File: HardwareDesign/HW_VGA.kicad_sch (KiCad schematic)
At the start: 6 parts, among them J1 Conn_02x40_Odd_Even, J401 Conn_01x06, U1 25.175 MHz, U301 GAL22V10

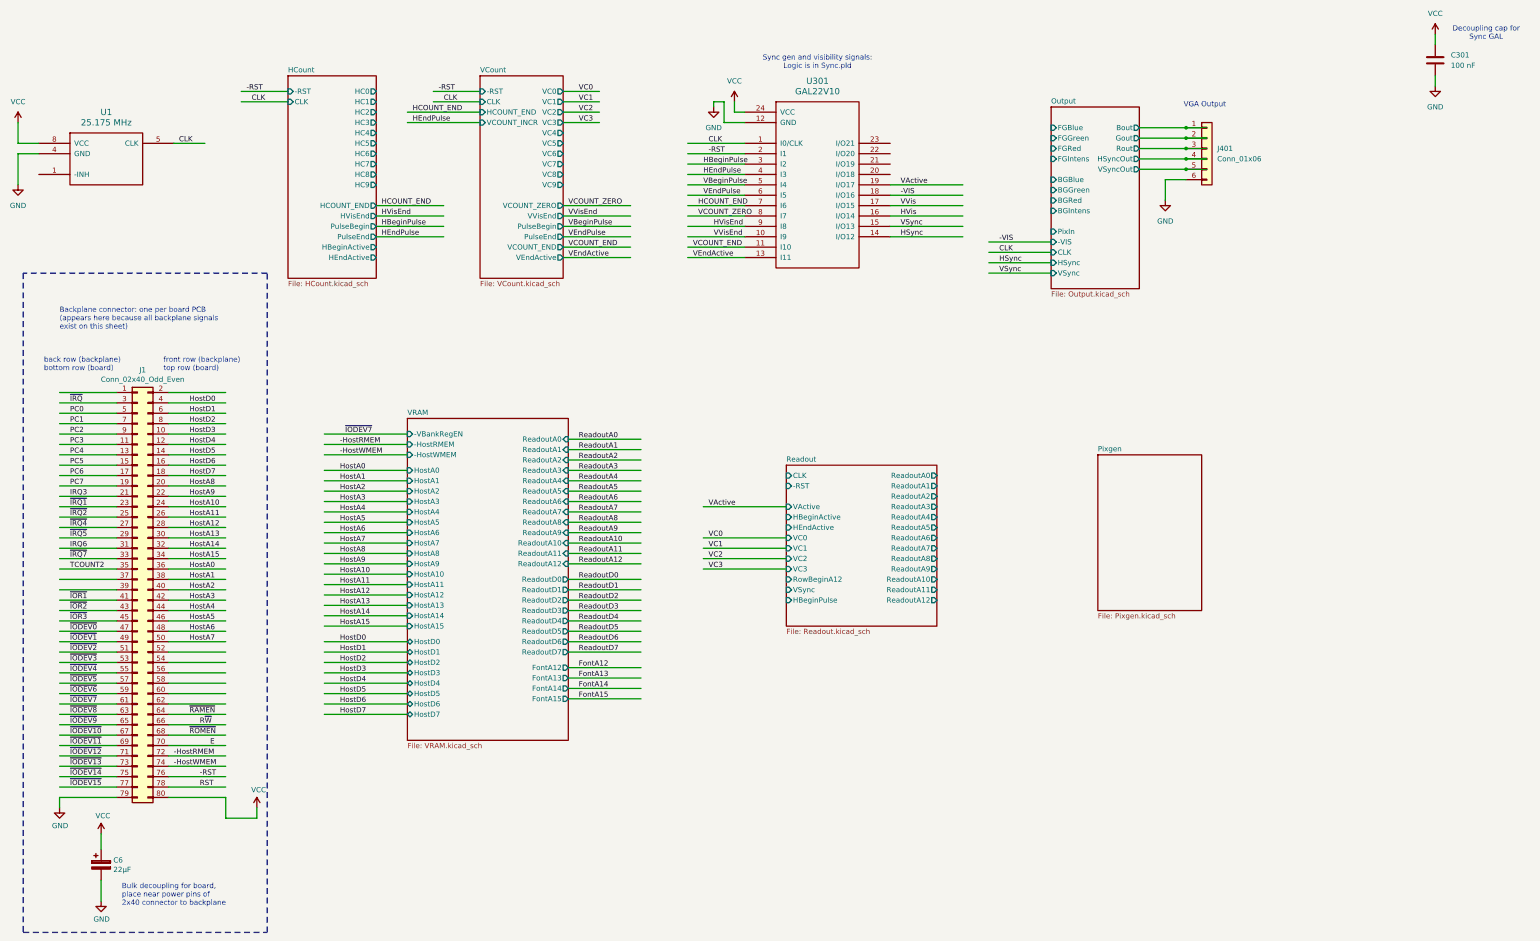
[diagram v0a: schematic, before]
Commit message: more main sheet cleanups
Also removed one unneeded pin (ReadoutA12) for the
Readout module: it's a purely internal signal.
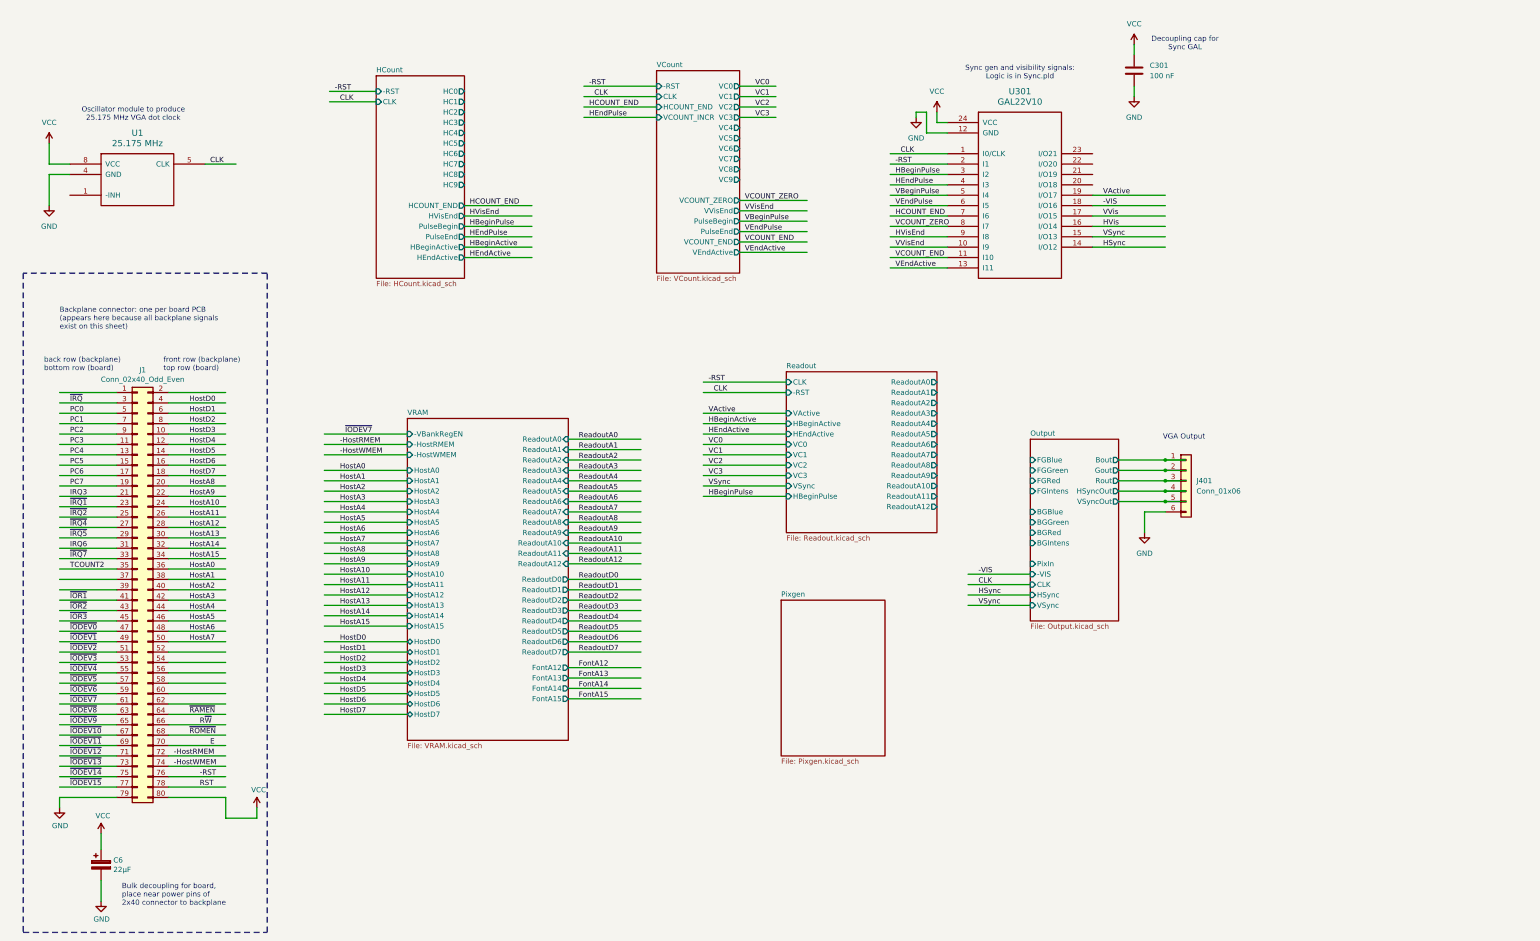
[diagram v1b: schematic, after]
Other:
- sheet Readout ports: added none; removed RowBeginA12
- note added: "Oscillator module to produce 25.175 MHz VGA dot clock"
- moved on the sheet: C301, J401, U1, U301

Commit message: a few more main sheet cleanups
At this point I think most/all of the changes to
the simulation are reflected in the schematic. Need
to go over everything carefully to make sure.
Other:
- note added: "Horizontal count"
- note added: "Readout module (generate addresses for reading character and attribute data from VRAM)"
- note added: "VRAM (video memory for character and attribute data)"
- note added: "Vertical count"
- moved on the sheet: J401, U1

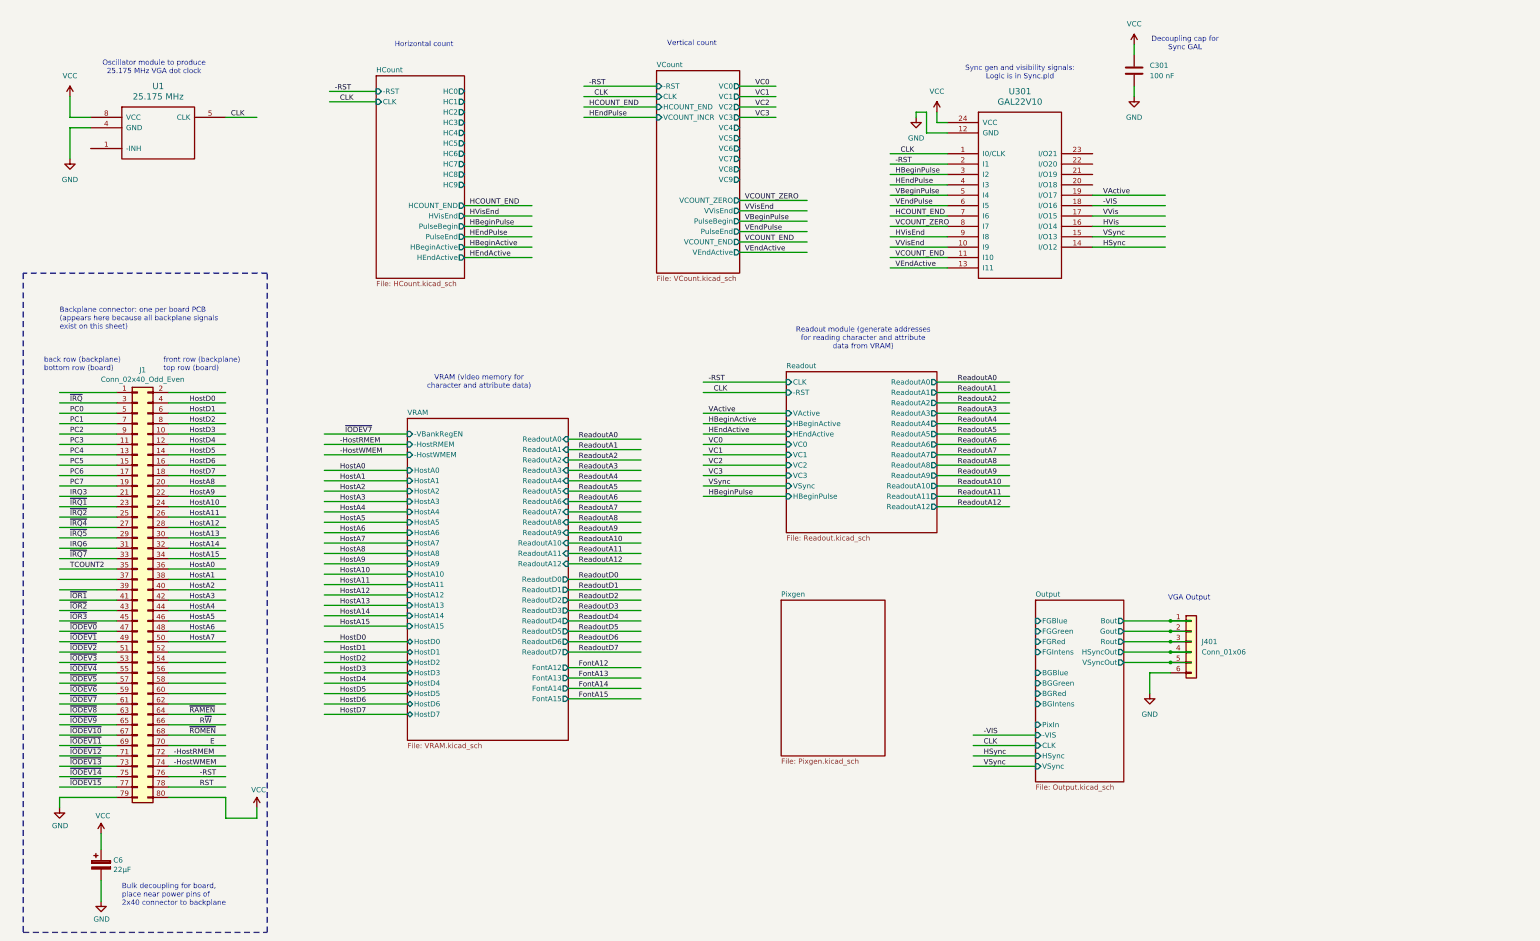
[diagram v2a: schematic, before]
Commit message: much work on pixel generation schematic, logic
In theory, this is potentially a complete hardware design,
but need to simulate it to make sure it will actually work.
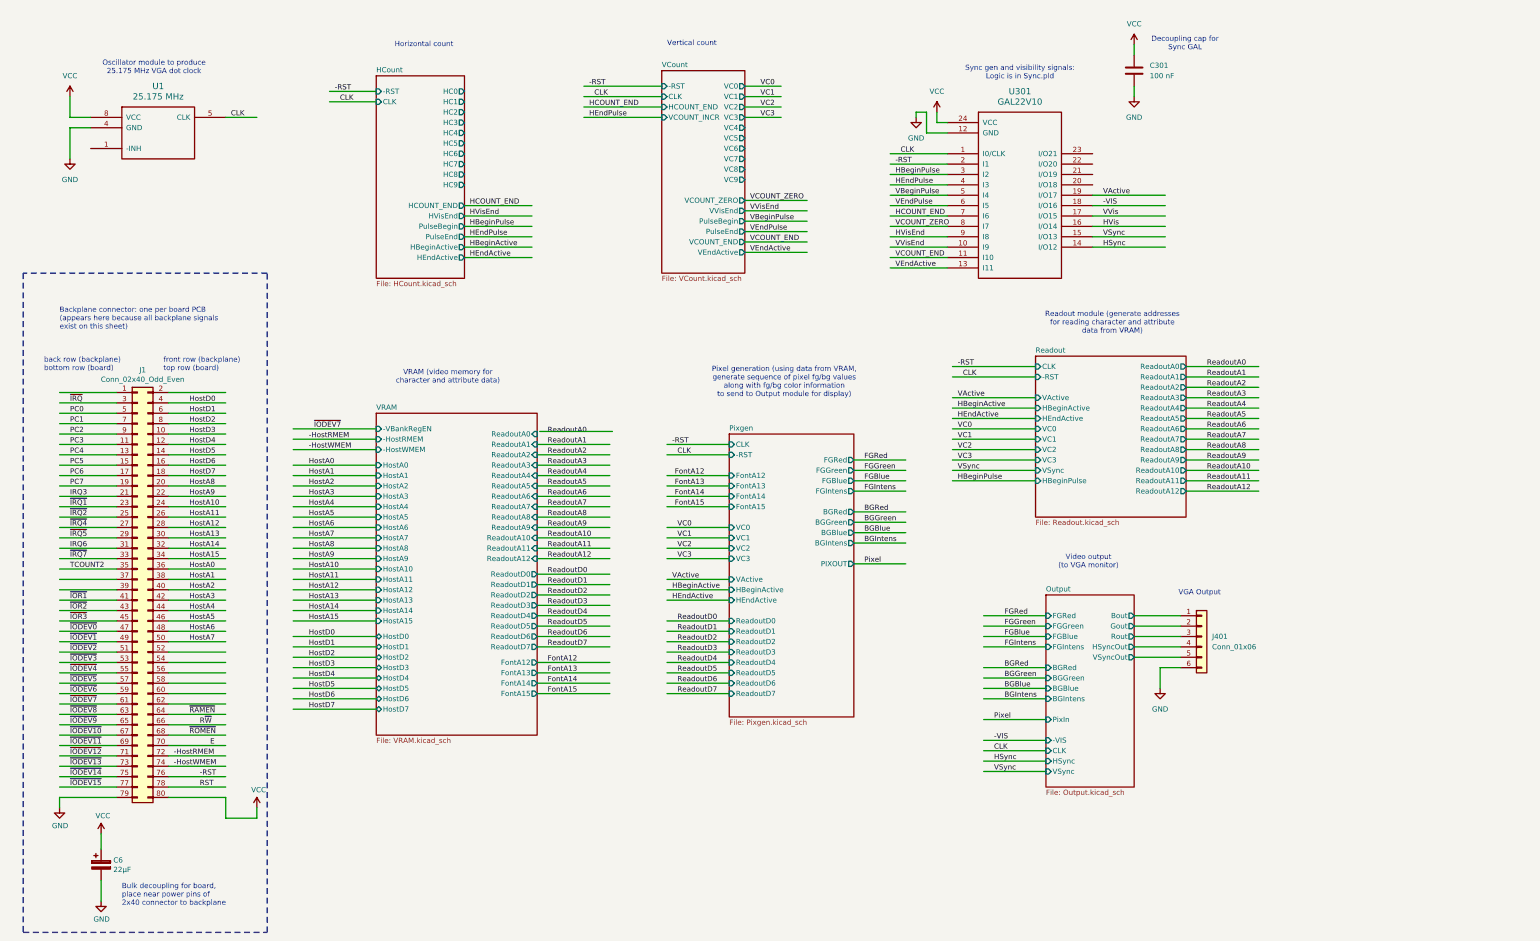
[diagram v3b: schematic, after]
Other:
- sheet Pixgen ports: added -RST, BGBlue, BGGreen, BGIntens, BGRed, CLK, FGBlue, FGGreen, FGIntens, FGRed, FontA12, FontA13, FontA14, FontA15, HBeginActive, HEndActive, PIXOUT, ReadoutD0, ReadoutD1, ReadoutD2, ReadoutD3, ReadoutD4, ReadoutD5, ReadoutD6, ReadoutD7, VActive, VC0, VC1, VC2, VC3; removed none
- note added: "Pixel generation (using data from VRAM, generate sequence of pixel fg/bg values along with fg/bg color information to send to Output module for display)"
- note added: "Video output (to VGA monitor)"
- moved on the sheet: J401

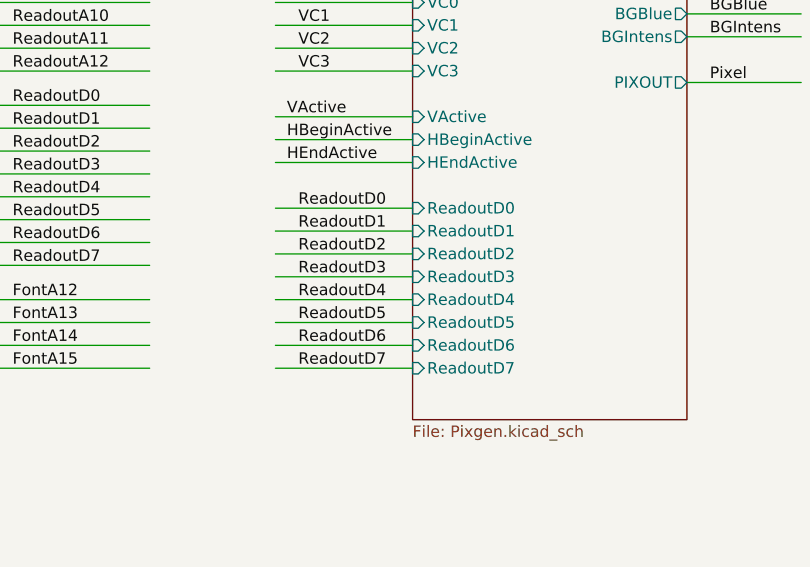
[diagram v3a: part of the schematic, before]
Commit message: updated schematic to send -VIS to Pixgen module
The Pixgen module should only shift data in the output
shift register if a visible pixel is being displayed.

Also, change Pixgen control GAL equations and simulation
to reflect -VIS being an active-low signal (they were
previously representing it as an active-high signal.)
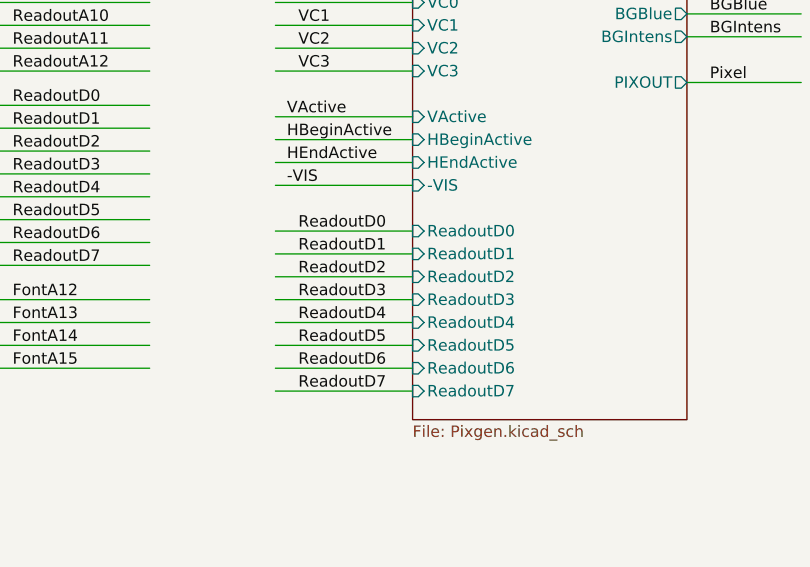
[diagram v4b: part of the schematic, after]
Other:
- sheet Pixgen ports: added -VIS; removed none
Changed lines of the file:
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@@
 	(wire
 		(pts
-			(xy 175.26 173.99) (xy 190.5 173.99)
+			(xy 175.26 176.53) (xy 190.5 176.53)
 		)
 		(stroke
@@
 	(wire
 		(pts
-			(xy 175.26 166.37) (xy 190.5 166.37)
+			(xy 175.26 168.91) (xy 190.5 168.91)
 		)
 		(stroke
@@
 	(wire
 		(pts
-			(xy 175.26 171.45) (xy 190.5 171.45)
+			(xy 175.26 173.99) (xy 190.5 173.99)
 		)
 		(stroke
@@
 	(wire
 		(pts
-			(xy 175.26 179.07) (xy 190.5 179.07)
+			(xy 175.26 181.61) (xy 190.5 181.61)
 		)
 		(stroke
@@
 	(wire
 		(pts
-			(xy 175.26 184.15) (xy 190.5 184.15)
+			(xy 175.26 186.69) (xy 190.5 186.69)
 		)
 		(stroke
@@
 	(wire
 		(pts
-			(xy 175.26 168.91) (xy 190.5 168.91)
+			(xy 175.26 171.45) (xy 190.5 171.45)
 		)
 		(stroke
@@
 	(wire
 		(pts
+			(xy 175.26 163.83) (xy 190.5 163.83)
+		)
+		(stroke
+			(width 0)
+			(type default)
+		)
+	)
+	(wire
+		(pts
 			(xy 26.67 153.67) (xy 40.64 153.67)
 		)
@@
 	(wire
 		(pts
-			(xy 175.26 181.61) (xy 190.5 181.61)
+			(xy 175.26 184.15) (xy 190.5 184.15)
 		)
 		(stroke
@@
 	(wire
 		(pts
-			(xy 175.26 176.53) (xy 190.5 176.53)
+			(xy 175.26 179.07) (xy 190.5 179.07)
 		)
 		(stroke
@@
 	)
 	(label "ReadoutD5"
-		(at 177.8 179.07 0)
+		(at 177.8 181.61 0)
 		(fields_autoplaced yes)
 		(effects
@@
 	)
 	(label "ReadoutD7"
-		(at 177.8 184.15 0)
+		(at 177.8 186.69 0)
 		(fields_autoplaced yes)
 		(effects
@@
 	)
 	(label "ReadoutD3"
-		(at 177.8 173.99 0)
+		(at 177.8 176.53 0)
 		(fields_autoplaced yes)
 		(effects
@@
 	)
 	(label "ReadoutD0"
-		(at 177.8 166.37 0)
+		(at 177.8 168.91 0)
 		(fields_autoplaced yes)
 		(effects
@@
 	)
 	(label "ReadoutD4"
-		(at 177.8 176.53 0)
+		(at 177.8 179.07 0)
 		(fields_autoplaced yes)
 		(effects
@@
 	)
 	(label "ReadoutD6"
-		(at 177.8 181.61 0)
+		(at 177.8 184.15 0)
 		(fields_autoplaced yes)
 		(effects
@@
 		)
 	)
+	(label "-VIS"
+		(at 176.53 163.83 0)
+		(fields_autoplaced yes)
+		(effects
+			(font
+				(size 1.27 1.27)
+			)
+			(justify left bottom)
+		)
+	)
 	(label "FGGreen"
 		(at 257.81 167.64 0)
@@
 	)
 	(label "ReadoutD1"
-		(at 177.8 168.91 0)
+		(at 177.8 171.45 0)
 		(fields_autoplaced yes)
 		(effects
@@
 	)
 	(label "ReadoutD2"
-		(at 177.8 171.45 0)
+		(at 177.8 173.99 0)
 		(fields_autoplaced yes)
 		(effects
@@
 		)
 		(pin "ReadoutD6" input
-			(at 190.5 181.61 180)
+			(at 190.5 184.15 180)
 			(effects
 				(font
@@
 		)
 		(pin "ReadoutD7" input
-			(at 190.5 184.15 180)
+			(at 190.5 186.69 180)
 			(effects
 				(font
@@
 		)
 		(pin "ReadoutD4" input
-			(at 190.5 176.53 180)
+			(at 190.5 179.07 180)
 			(effects
 				(font
@@
 		)
 		(pin "ReadoutD3" input
-			(at 190.5 173.99 180)
+			(at 190.5 176.53 180)
 			(effects
 				(font
@@
 		)
 		(pin "ReadoutD0" input
-			(at 190.5 166.37 180)
+			(at 190.5 168.91 180)
 			(effects
 				(font
@@
 		)
 		(pin "ReadoutD2" input
-			(at 190.5 171.45 180)
+			(at 190.5 173.99 180)
 			(effects
 				(font
@@
 		)
 		(pin "ReadoutD5" input
-			(at 190.5 179.07 180)
+			(at 190.5 181.61 180)
 			(effects
 				(font
@@
 		)
 		(pin "ReadoutD1" input
-			(at 190.5 168.91 180)
+			(at 190.5 171.45 180)
 			(effects
 				(font
@@
 			(effects
 				(font
+					(size 1.27 1.27)
+				)
+				(justify left)
+			)
+		)
+		(pin "-VIS" input
+			(at 190.5 163.83 180)
+			(effects
+				(font

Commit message: generate vertical refresh interrupt as IRQ6
The Sync GAL can do this very easily. Not tested yet.
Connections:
- net IRQ6: now also U301.20 (I/O18)
- net VActPrev: now reaches U301.21 (I/O19)
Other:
- note added: "Note that pin 20 is a one-cycle vertical refresh pulse, which is sent to the interrupt controller as the edge-triggered IRQ6."
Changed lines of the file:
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@@
 	(wire
 		(pts
+			(xy 279.4 57.15) (xy 297.18 57.15)
+		)
+		(stroke
+			(width 0)
+			(type default)
+		)
+	)
+	(wire
+		(pts
 			(xy 289.56 167.64) (xy 300.99 167.64)
 		)
@@
 	(wire
 		(pts
+			(xy 279.4 59.69) (xy 297.18 59.69)
+		)
+		(stroke
+			(width 0)
+			(type default)
+		)
+	)
+	(wire
+		(pts
 			(xy 279.4 72.39) (xy 297.18 72.39)
 		)
@@
 		)
 	)
+	(text "Note that pin 20 is a one-cycle\nvertical refresh pulse, which is\nsent to the interrupt controller\nas the edge-triggered IRQ6."
+		(exclude_from_sim no)
+		(at 304.8 51.054 0)
+		(effects
+			(font
+				(size 1.27 1.27)
+			)
+		)
+	)
 	(text "Sync gen and visibility signals:\nLogic is in Sync.pld"
 		(exclude_from_sim no)
@@
 		)
 	)
+	(label "IRQ6"
+		(at 281.94 59.69 0)
+		(fields_autoplaced yes)
+		(effects
+			(font
+				(size 1.27 1.27)
+			)
+			(justify left bottom)
+		)
+	)
 	(label "VCOUNT_END"
 		(at 195.58 73.66 0)
@@
 		(fields_autoplaced yes)
 		(effects
+			(font
+				(size 1.27 1.27)
+			)
+			(justify left bottom)
+		)
+	)
+	(label "VActPrev"
+		(at 281.94 57.15 0)
+		(fields_autoplaced yes)
+		(effects
